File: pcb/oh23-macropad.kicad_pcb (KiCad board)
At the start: 2 copper layers, 64.8 x 24 mm, 5 parts, among them J1 Conn_01x11, SW1 SW_Push, SW2 SW_Push, SW3 SW_Push, U1 MOUDLE-SEEEDUINO-XIAO

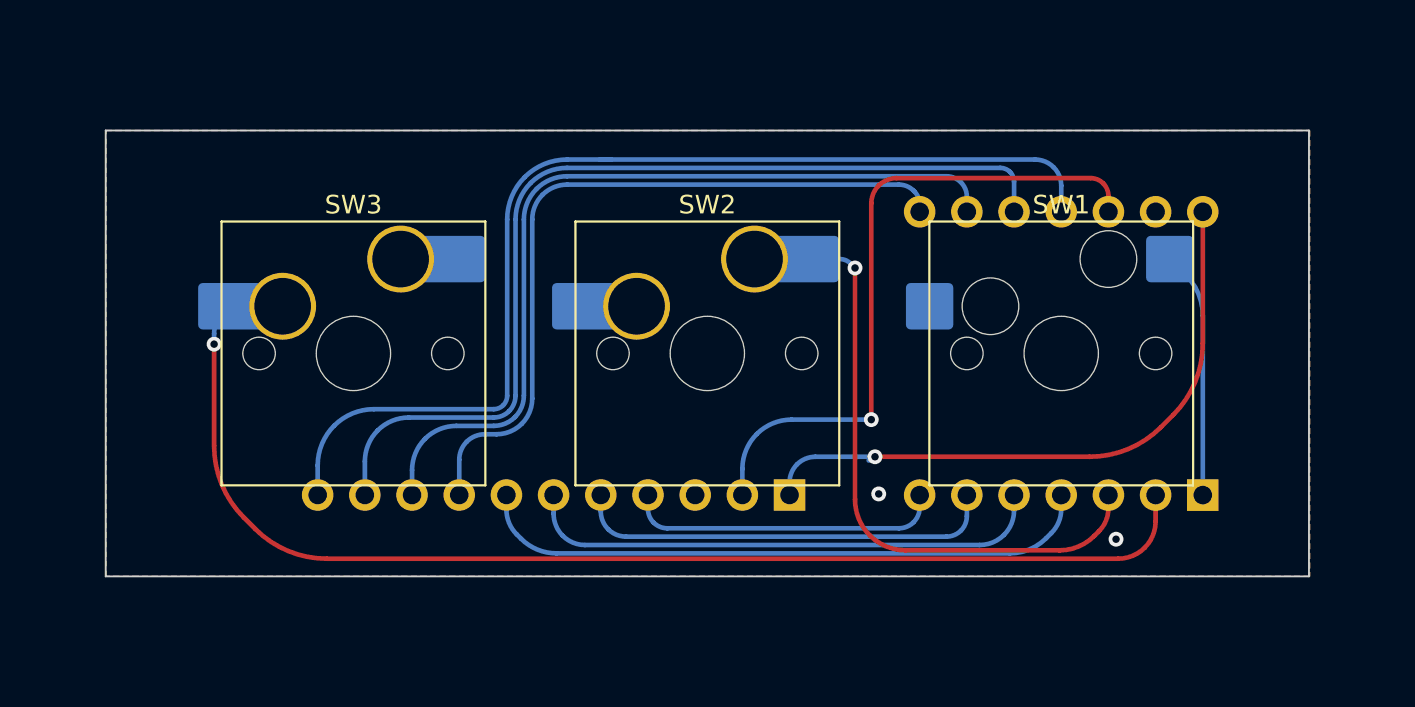
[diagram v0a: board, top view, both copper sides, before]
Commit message: Add more design, separate plate and pcb file
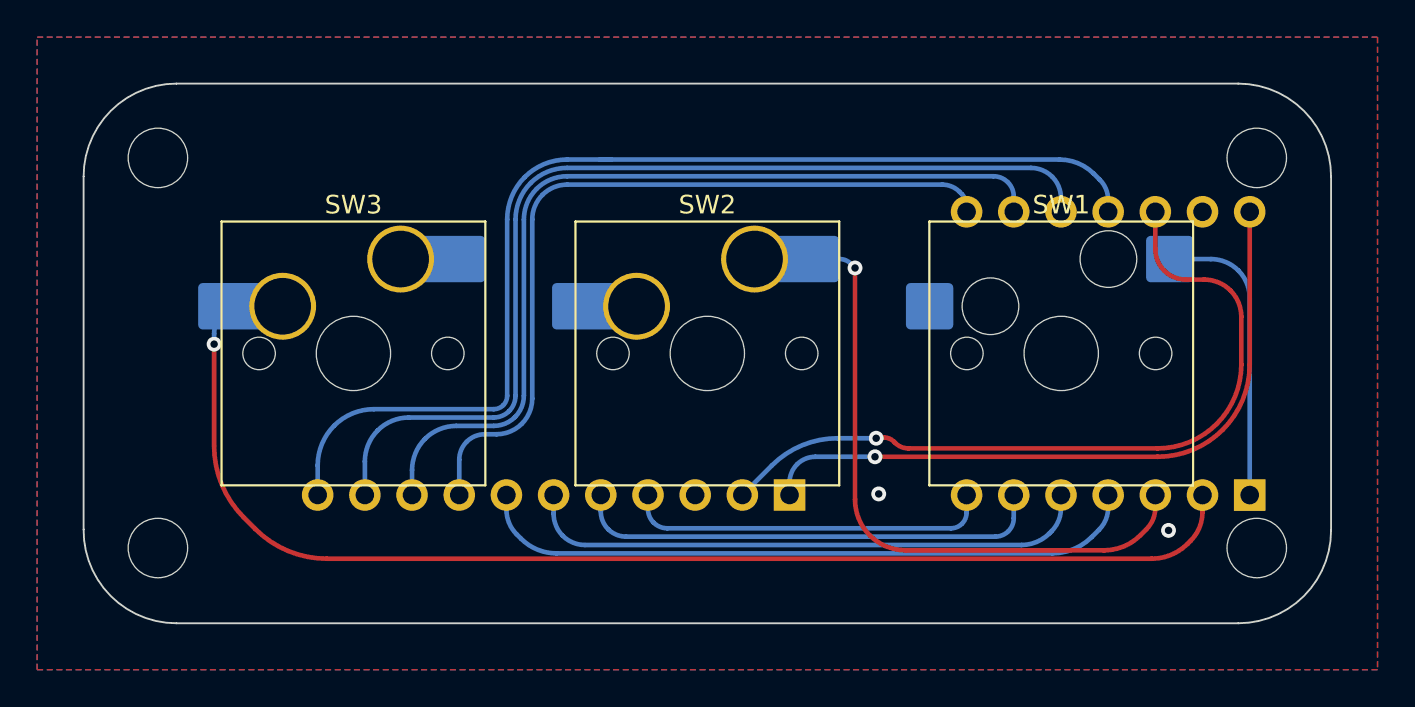
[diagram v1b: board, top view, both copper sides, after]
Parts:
- added H1: MountingHole, MountingHole:MountingHole_3.2mm_M3, F.Cu at (128.5, 82.2)
- added H2: MountingHole, MountingHole:MountingHole_3.2mm_M3, F.Cu at (128.5, 103.2)
- added H3: MountingHole, MountingHole:MountingHole_3.2mm_M3, F.Cu at (69.4, 82.2)
- added H4: MountingHole, MountingHole:MountingHole_3.2mm_M3, F.Cu at (69.4, 103.2)
- moved U1 2.53 mm to (120.5, 92.8)
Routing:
- net +3V3: track 36.4 -> 41.8 mm
- net +5V: track 34.5 -> 37.4 mm
- net Net-(SW1-Pad2): track 13.3 -> 16.0 mm
- net /GP00_D06: track 17.3 -> 19.9 mm
- net /GP07_D05: track 23.1 -> 25.7 mm
- net /GP02_D08: track 45.7 -> 48.2 mm
- net Net-(SW2-Pad2): track 32.3 -> 34.8 mm
- net /GP01_D07: track 40.2 -> 42.7 mm
- net /GP29_D03: track 33.8 -> 36.3 mm
- net /GP06_D04: track 28.6 -> 31.0 mm
- net Net-(SW3-Pad1): track 64.4 -> 66.6 mm
- net /GP04_D09: track 51.8 -> 54.0 mm
- net /GP03_D10: track 57.8 -> 59.9 mm
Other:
- board size 64.8 x 24 mm -> 67.2 x 29.1 mm

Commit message: Wire up extra microcontroller pins to a header, align mounting holes
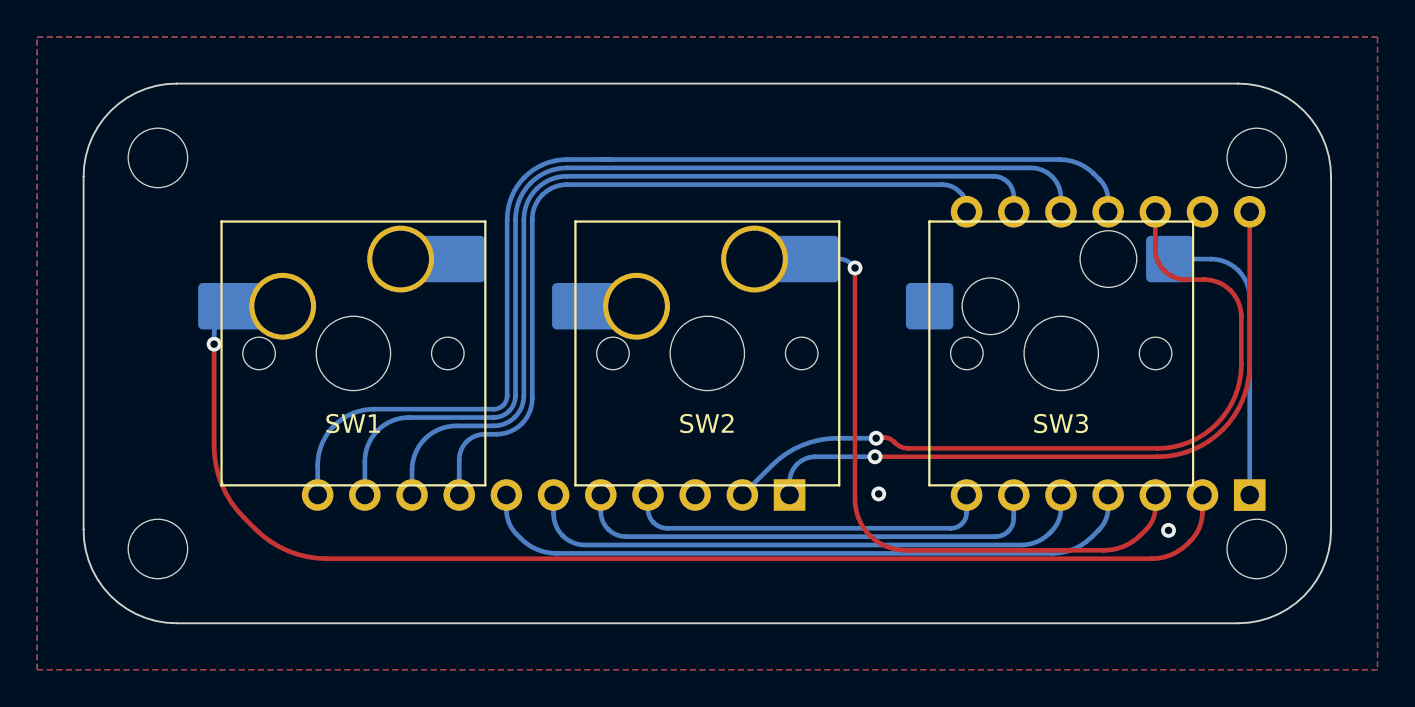
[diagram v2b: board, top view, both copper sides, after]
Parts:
- SW1: footprint Switch_Keyboard_Hotswap_Kailh:SW_Hotswap_Kailh_MX_1.00u -> Switch_Keyboard_Hotswap_Kailh:SW_Hotswap_Kailh_MX_plated_1.00u
- SW3: footprint Switch_Keyboard_Hotswap_Kailh:SW_Hotswap_Kailh_MX_plated_1.00u -> Switch_Keyboard_Hotswap_Kailh:SW_Hotswap_Kailh_MX_1.00u
- moved SW1 38.1 mm to (79.9, 92.8)
- moved SW3 38.1 mm to (118.0, 92.8)
- moved H2 0.05 mm to (128.5, 103.3)
- moved H4 0.05 mm to (69.4, 103.3)
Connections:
- SW1 pad 1: GND -> Net-(SW1-Pad1)
- SW1 pad 2: Net-(SW1-Pad2) -> GND
- SW3 pad 1: Net-(SW3-Pad1) -> GND
- SW3 pad 2: GND -> Net-(U1-Pad1)
- U1 pad 1: Net-(SW1-Pad2) -> Net-(U1-Pad1)
- U1 pad 2: Net-(SW3-Pad1) -> Net-(SW1-Pad1)
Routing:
- net Net-(SW3-Pad1): track 66.6 -> 0.00 mm, vias 1 -> 0
- net Net-(SW1-Pad1): track 0.00 -> 66.6 mm, vias 0 -> 1
- net Net-(U1-Pad1): track 0.00 -> 16.0 mm
- net Net-(SW1-Pad2): track 16.0 -> 0.00 mm
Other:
- board text added: "3-KEY MACROPAD"
- board text added: "For info on programming, etc: kaine119.github.io/oh23-macropad"
- board text added: "GP00"
- board text added: "GP01"
- board text added: "GP02"
- board text added: "GP03"
- board text added: "GP04"
- board text added: "GP06"
- board text added: "GP07"
- board text added: "I2C_1"
- board text added: "SPI_0"
- board text added: "SUTD Keyboard Warriors presents a"
- board text added: "for all your ctrl-c & ctrl-v needs"
- board text removed: "3-key Macropad"
- board text removed: "GP0"
- board text removed: "GP1"
- board text removed: "GP2"
- board text removed: "GP3"
- board text removed: "GP4"
- board text removed: "GP6"
- board text removed: "GP7"
- board text removed: "I2C1"
- board text removed: "SPI0"

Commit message: move microcontroller back to dodge hex standoffs
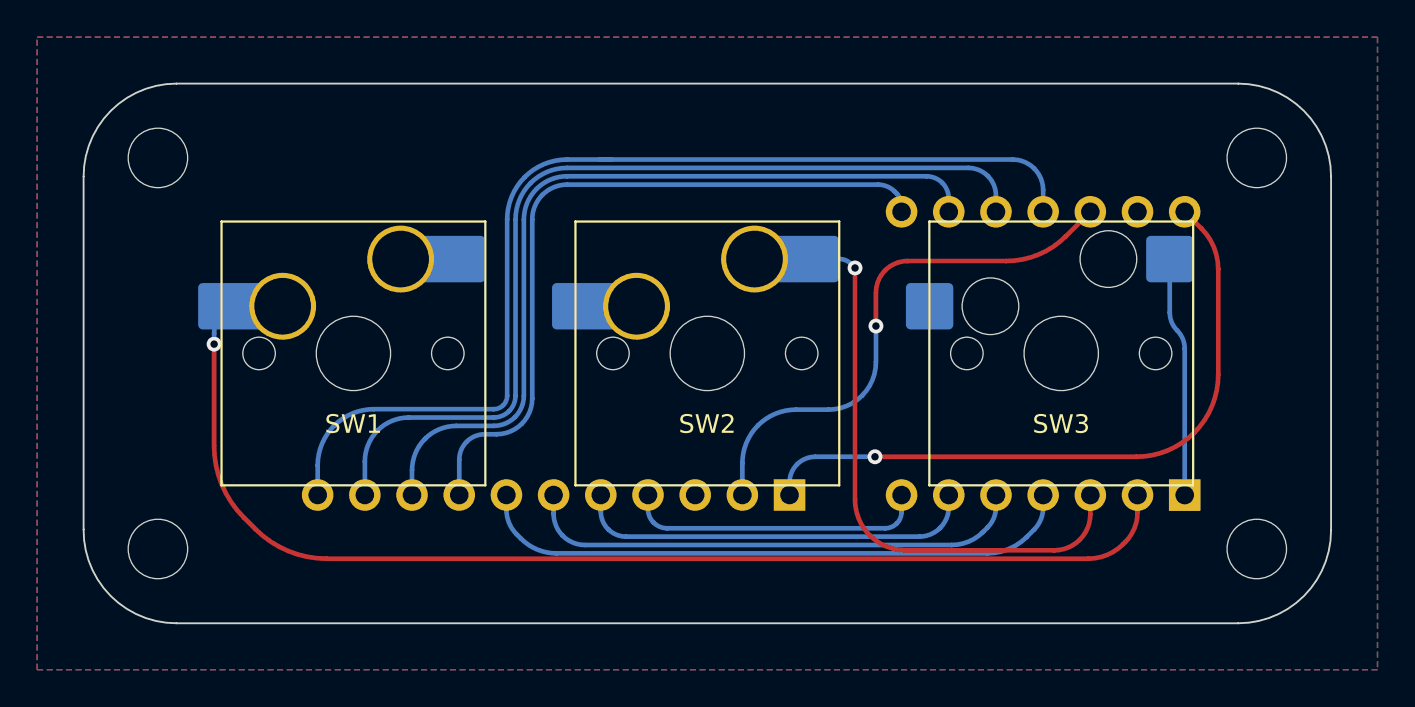
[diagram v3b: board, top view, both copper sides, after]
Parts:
- moved U1 3.50 mm to (117.0, 92.8)
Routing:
- net +3V3: track 41.8 -> 29.1 mm
- net /GP07_D05: track 25.7 -> 21.9 mm
- net /GP06_D04: track 31.0 -> 27.4 mm
- net /GP02_D08: track 48.2 -> 44.6 mm
- net /GP00_D06: track 19.9 -> 16.4 mm
- net /GP29_D03: track 36.3 -> 32.8 mm
- net /GP01_D07: track 42.7 -> 39.2 mm
- net Net-(SW1-Pad1): track 66.6 -> 63.1 mm
- net /GP04_D09: track 54.0 -> 50.5 mm
- net Net-(SW2-Pad2): track 34.8 -> 31.6 mm
- net /GP03_D10: track 59.9 -> 56.7 mm
- net Net-(U1-Pad1): track 16.0 -> 13.5 mm
- net +5V: track 37.2 -> 36.4 mm
- net GND: vias 2 -> 0
